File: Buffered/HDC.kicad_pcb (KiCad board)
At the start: 2 copper layers, 84.3 x 56.6 mm, 19 parts, among them J1 Spectrum 128/Grey +2 edge con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, J2 HDD_LED, J3 POWER, J4 PATA_40, J5 DOM_POWER_ENABLE, Q1 BC327, U1 74LS245, U2 74LS245, U3 74LS10

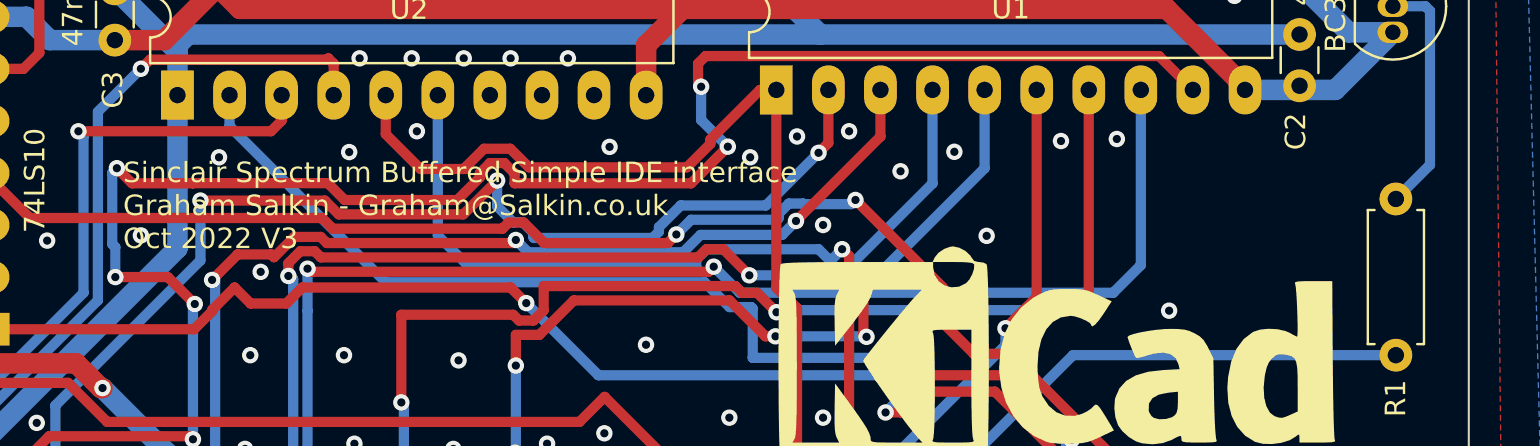
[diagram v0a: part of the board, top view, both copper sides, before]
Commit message: Fixed the silk screen on the buffered version to properly credit the original designers.
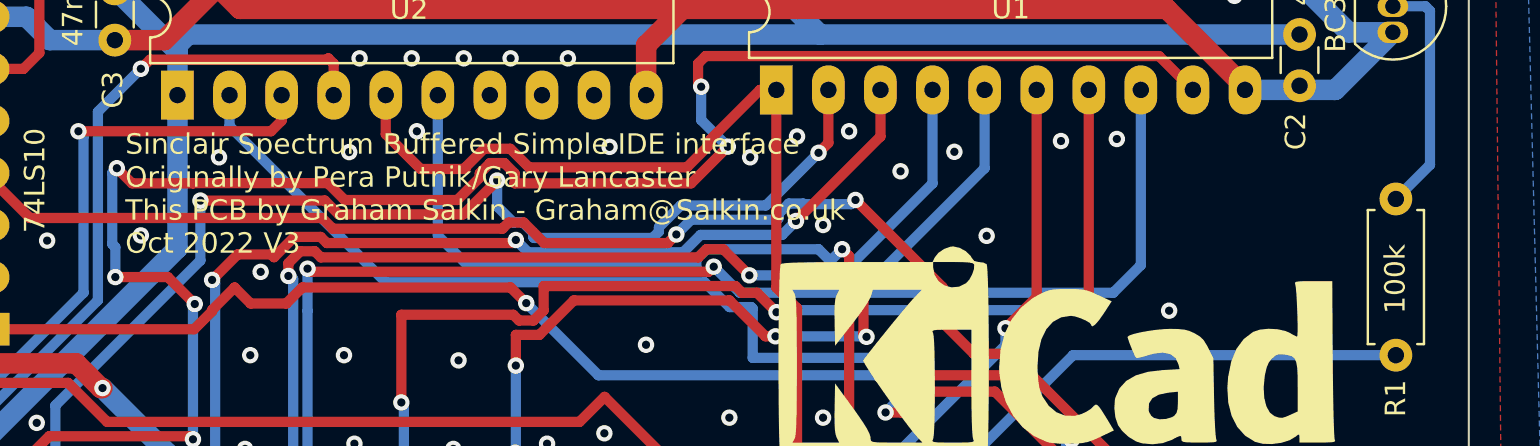
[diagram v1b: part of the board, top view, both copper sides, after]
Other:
- board text added: "Sinclair Spectrum Buffered Simple IDE interface Originally by Pera Putnik/Gary Lancaster This PCB by Graham Salkin - Graham@Salkin.co.uk Oct 2022 V3"
- board text removed: "Sinclair Spectrum Buffered Simple IDE interface Graham Salkin - Graham@Salkin.co.uk Oct 2022 V3"
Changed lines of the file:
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@@
       (effects (font (size 1 1) (thickness 0.15)))
     )
-    (fp_text value "100k" (at 3.72 -0.036 90) (layer "F.Fab")
+    (fp_text value "100k" (at 3.72 -0.036 90) (layer "F.SilkS")
       (effects (font (size 1 1) (thickness 0.15)))
     )
@@
   (gr_line (start 173.736 147.574) (end 177.292 147.574) (layer "Edge.Cuts") (width 0.1))
   (gr_line (start 92.964 147.828) (end 97.028 147.828) (layer "Edge.Cuts") (width 0.1))
-  (gr_text "Sinclair Spectrum Buffered Simple IDE interface\nGraham Salkin - Graham@Salkin.co.uk\nOct 2022 V3 " (at 111.65 133.675) (layer "F.SilkS")
+  (gr_text "Sinclair Spectrum Buffered Simple IDE interface\nOriginally by Pera Putnik/Gary Lancaster\nThis PCB by Graham Salkin - Graham@Salkin.co.uk\nOct 2022 V3 " (at 111.76 133.096) (layer "F.SilkS")
     (effects (font (size 1 1) (thickness 0.15)) (justify left))
   )
